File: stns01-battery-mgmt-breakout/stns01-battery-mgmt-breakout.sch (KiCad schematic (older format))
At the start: 0 parts

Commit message: Create schematic.
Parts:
- added B1: 3.7V, Wickerlib:UNDEFINED, symbol BATT-LIPO-3.7V-500MAH-JST-2PIN
- added C1, C3, C4: 2.2uF, Wickerlib:RLC-0603-SMD, symbol CAP-CER-2.2UF-10V-X7R-0603
- added C2: 4.7uF, Wickerlib:RLC-0603-SMD, symbol CAP-CER-4.7UF-6.3V-X7R-0603
- added J1: MICRO USB, Wickerlib:CONN-USB-MICRO-B-AMPHENOL-10118193-0001LF, symbol CONN-USB-MICRO-B-10118193
- added J2: PH, Wickerlib:CONN-JST-S2B-PH-SM4-TB, symbol HEADER-FEMALE-2POS-TH-1x02-JST-PH
- added J3: POWER PINS, Wickerlib:CONN-HEADER-STRAIGHT-P2.54MM-1x07, symbol HEADER-MALE-7POS-TH-1x07-P0.1IN
- added J4: CONTROL PINS, Wickerlib:CONN-HEADER-STRAIGHT-P2.54MM-1x07, symbol HEADER-MALE-7POS-TH-1x07-P0.1IN
- added LED1: RED, Wickerlib:LED-0603-SMD, symbol LED-RED-0603-SMT-HSMS-C191
- added R1: 0 ohm, Wickerlib:RLC-0603-SMD, symbol RES-0.0-JUMPER-1/8W-0603
- added R2, R5, R6: 10K, Wickerlib:RLC-0603-SMD, symbol RES-10K-1%-1/8W-0603
- added R3: NTC 10K, Wickerlib:RLC-0402-SMD, symbol THERM-NTC-10K-1%-0402
- added R4: 604, Wickerlib:RLC-0603-SMD, symbol RES-604-OHM-1%-1/10W-0603
- added S1: SHUNT, Wickerlib:CONN-HEADER-STRAIGHT-P2.54MM-1x03, symbol SWITCH_JUMPER_3PIN
- added S2: SLIDE, Wickerlib:SWITCH-ESWITCH-SLIDE-TH-EG1218, symbol SWITCH-SLIDE-SPDT-200MA-30V
- added U1: STNS01, Wickerlib:DFN-12-1EP-3x3MM-P0.45MM, symbol IC-LI-ION-BATT-CHARGER-LDO-STNS01-DFN12
- added U2: LDO REG 3.3V, Wickerlib:SOT-23-3, symbol IC-REG-LDO-3.3V-0.25A-MCP1703-SOT23A-3
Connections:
- net labels added: 3.1V, 3.3V, BAT_CEN, BAT_MS, BAT_NTC, BAT_SD, GND, LDO, SYS, TRANS, VBAT, VCC, VUSB, ~BAT_CHG
- wire segments 0 -> 57
- no-connect marks 0 -> 6
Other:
- note added: "100mA"
- note added: "250mA"
- note added: "BATTERY"
- note added: "BATTERY CONTROL"
- note added: "ON/OFF\nSWITCH"
- note added: "SYS is 5V with USB applied"
- note added: "TODO: 0603 NTC 10K"
- note added: "TODO: see if this is optional"
- note added: "USB"
- note added: "VOLTAGE \nREGULATOR"

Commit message: Generate BOM. Initial parts placement.
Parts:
- removed R3: NTC 10K, Wickerlib:RLC-0402-SMD, symbol THERM-NTC-10K-1%-0402
- added R3: NTC 10K, Wickerlib:RLC-0603-SMD, symbol THERM-NTC-10K-5%-0603
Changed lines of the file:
@@
 $EndComp
 $Comp
-L VUSB #PWR01
+L VUSB #PWR2
 U 1 1 58F8E338
 P 1700 1700
-F 0 "#PWR01" H 1700 1550 50  0001 C CNN
+F 0 "#PWR2" H 1700 1550 50  0001 C CNN
 F 1 "VUSB" H 1700 1840 50  0000 C CNN
 F 2 "" H 1700 1700 50  0000 C CNN
@@
 $EndComp
 $Comp
-L GND #PWR02
+L GND #PWR1
 U 1 1 58F8E351
 P 1625 2275
-F 0 "#PWR02" H 1625 2025 50  0001 C CNN
+F 0 "#PWR1" H 1625 2025 50  0001 C CNN
 F 1 "GND" H 1625 2125 50  0000 C CNN
 F 2 "" H 1625 2275 50  0000 C CNN
@@
 $EndComp
 $Comp
-L VBAT #PWR03
+L VBAT #PWR4
 U 1 1 58F8E938
 P 2700 2250
-F 0 "#PWR03" H 2700 2100 50  0001 C CNN
+F 0 "#PWR4" H 2700 2100 50  0001 C CNN
 F 1 "VBAT" H 2700 2390 50  0000 C CNN
 F 2 "" H 2700 2250 50  0000 C CNN
@@
 $EndComp
 $Comp
-L GND #PWR04
+L GND #PWR15
 U 1 1 58FA8587
 P 6725 2125
-F 0 "#PWR04" H 6725 1875 50  0001 C CNN
+F 0 "#PWR15" H 6725 1875 50  0001 C CNN
 F 1 "GND" H 6725 1975 50  0000 C CNN
 F 2 "" H 6725 2125 50  0000 C CNN
@@
 USB
 $Comp
-L GND #PWR05
+L GND #PWR5
 U 1 1 58FE6662
 P 2700 2700
-F 0 "#PWR05" H 2700 2450 50  0001 C CNN
+F 0 "#PWR5" H 2700 2450 50  0001 C CNN
 F 1 "GND" H 2700 2550 50  0000 C CNN
 F 2 "" H 2700 2700 50  0000 C CNN
@@
 $EndComp
 $Comp
-L GND #PWR06
+L GND #PWR3
 U 1 1 59019EDC
 P 2200 2150
-F 0 "#PWR06" H 2200 1900 50  0001 C CNN
+F 0 "#PWR3" H 2200 1900 50  0001 C CNN
 F 1 "GND" H 2200 2000 50  0000 C CNN
 F 2 "" H 2200 2150 50  0000 C CNN
@@
 $EndComp
 $Comp
-L GND #PWR07
+L GND #PWR8
 U 1 1 5901E800
 P 3750 2975
-F 0 "#PWR07" H 3750 2725 50  0001 C CNN
+F 0 "#PWR8" H 3750 2725 50  0001 C CNN
 F 1 "GND" H 3750 2825 50  0000 C CNN
 F 2 "" H 3750 2975 50  0000 C CNN
@@
 $EndComp
 $Comp
-L GND #PWR08
+L GND #PWR7
 U 1 1 59022473
 P 3500 2975
-F 0 "#PWR08" H 3500 2725 50  0001 C CNN
+F 0 "#PWR7" H 3500 2725 50  0001 C CNN
 F 1 "GND" H 3500 2825 50  0000 C CNN
 F 2 "" H 3500 2975 50  0000 C CNN
@@
 $EndComp
 $Comp
-L GND #PWR09
+L GND #PWR10
 U 1 1 59024679
 P 5650 2200
-F 0 "#PWR09" H 5650 1950 50  0001 C CNN
+F 0 "#PWR10" H 5650 1950 50  0001 C CNN
 F 1 "GND" H 5650 2050 50  0000 C CNN
 F 2 "" H 5650 2200 50  0000 C CNN
@@
 $EndComp
 $Comp
-L GND #PWR010
+L GND #PWR13
 U 1 1 59024867
 P 6050 2200
-F 0 "#PWR010" H 6050 1950 50  0001 C CNN
+F 0 "#PWR13" H 6050 1950 50  0001 C CNN
 F 1 "GND" H 6050 2050 50  0000 C CNN
 F 2 "" H 6050 2200 50  0000 C CNN
@@
 Text Label 4800 2825 0    50   ~ 0
 BAT_SD
-$Comp
-L THERM-NTC-10K-1%-0402 R3
-U 1 1 5902A870
-P 4825 3100
-F 0 "R3" H 4875 3150 50  0000 L CNN
-F 1 "NTC 10K" H 4875 3050 50  0000 L CNN
-F 2 "Wickerlib:RLC-0402-SMD" H 4825 2750 50  0001 C CIN
-F 3 "https://product.tdk.com/info/en/catalog/datasheets/tpd_ntc-thermistor_ntcg_en.pdf" H 4825 3100 5   0001 C CNN
-F 4 "NTC THERMISTOR 10K OHM 1% 0402" H 4825 2750 50  0001 C CIN "Description"
-F 5 "Samsung" H 4825 2750 50  0001 C CIN "MF_Name"
-F 6 "NTCG103JF103FT1" H 4825 2750 50  0001 C CIN "MF_PN"
-F 7 "Digikey" H 4825 2750 50  0001 C CIN "S1_Name"
-F 8 "445-2550-1-ND" H 4825 2750 50  0001 C CIN "S1_PN"
-	1    4825 3100
-	1    0    0    -1
-$EndComp
 $Comp
 L CAP-CER-4.7UF-6.3V-X7R-0603 C2
@@
 $EndComp
 $Comp
-L GND #PWR011
+L GND #PWR9
 U 1 1 5902C4A7
 P 4825 3200
-F 0 "#PWR011" H 4825 2950 50  0001 C CNN
+F 0 "#PWR9" H 4825 2950 50  0001 C CNN
 F 1 "GND" H 4825 3050 50  0000 C CNN
 F 2 "" H 4825 3200 50  0000 C CNN
@@
 $EndComp
 $Comp
-L GND #PWR012
+L GND #PWR6
 U 1 1 5903DF61
 P 3175 2600
-F 0 "#PWR012" H 3175 2350 50  0001 C CNN
+F 0 "#PWR6" H 3175 2350 50  0001 C CNN
 F 1 "GND" H 3175 2450 50  0000 C CNN
 F 2 "" H 3175 2600 50  0000 C CNN
@@
 $EndComp
 $Comp
-L VCC #PWR013
+L VCC #PWR16
 U 1 1 5906674F
 P 9100 1850
-F 0 "#PWR013" H 9100 1700 50  0001 C CNN
+F 0 "#PWR16" H 9100 1700 50  0001 C CNN
 F 1 "VCC" H 9100 1990 50  0000 C CNN
 F 2 "" H 9100 1850 50  0000 C CNN
@@
 	5775 5000 5775 5100
 $Comp
-L GND #PWR014
+L GND #PWR11
 U 1 1 5970EEFD
 P 5775 5100
-F 0 "#PWR014" H 5775 4850 50  0001 C CNN
+F 0 "#PWR11" H 5775 4850 50  0001 C CNN
 F 1 "GND" H 5775 4950 50  0000 C CNN
 F 2 "" H 5775 5100 50  0000 C CNN
@@
 	4750 5000 5100 5000
 $Comp
-L VCC #PWR015
+L VCC #PWR12
 U 1 1 59713110
 P 5800 4300
-F 0 "#PWR015" H 5800 4150 50  0001 C CNN
+F 0 "#PWR12" H 5800 4150 50  0001 C CNN
 F 1 "VCC" H 5800 4440 50  0000 C CNN
 F 2 "" H 5800 4300 50  0000 C CNN
@@
 $EndComp
 $Comp
-L GND #PWR016
+L GND #PWR14
 U 1 1 5971494F
 P 6125 3425
-F 0 "#PWR016" H 6125 3175 50  0001 C CNN
+F 0 "#PWR14" H 6125 3175 50  0001 C CNN
 F 1 "GND" H 6125 3275 50  0000 C CNN
 F 2 "" H 6125 3425 50  0000 C CNN
@@
 	1    0    0    -1
 $EndComp
+$Comp
+L THERM-NTC-10K-5%-0603 R3
+U 1 1 59715C0B
+P 4825 3100
+F 0 "R3" H 4875 3150 50  0000 L CNN
+F 1 "NTC 10K" H 4875 3050 50  0000 L CNN
+F 2 "Wickerlib:RLC-0603-SMD" H 4825 2750 50  0001 C CIN
+F 3 "https://product.tdk.com/info/en/catalog/datasheets/tpd_ntc-thermistor_ntcg_en.pdf" H 4825 3100 5   0001 C CNN
+F 4 "NTC THERMISTOR 10K OHM 5% 0603" H 4825 2750 50  0001 C CIN "Description"
+F 5 "TDK" H 4825 2750 50  0001 C CIN "MF_Name"
+F 6 "NTCG164BH103JT1" H 4825 2750 50  0001 C CIN "MF_PN"
+F 7 "Digikey" H 4825 2750 50  0001 C CIN "S1_Name"
+F 8 "445-174327-1-ND" H 4825 2750 50  0001 C CIN "S1_PN"
+	1    4825 3100
+	1    0    0    -1
+$EndComp

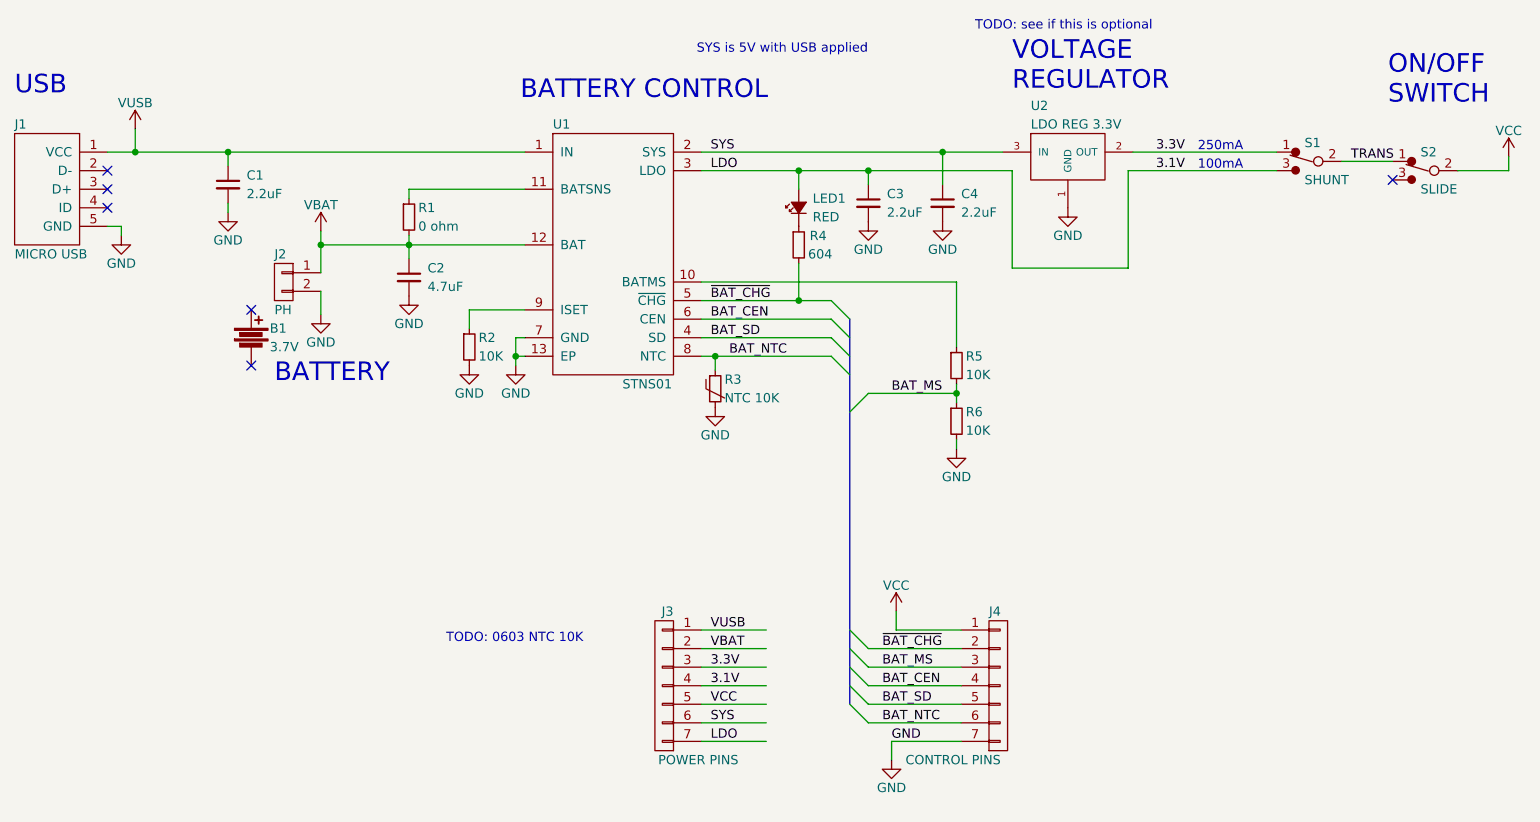
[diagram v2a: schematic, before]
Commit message: Release v1.0 STNS01 battery breakout, needs tested.
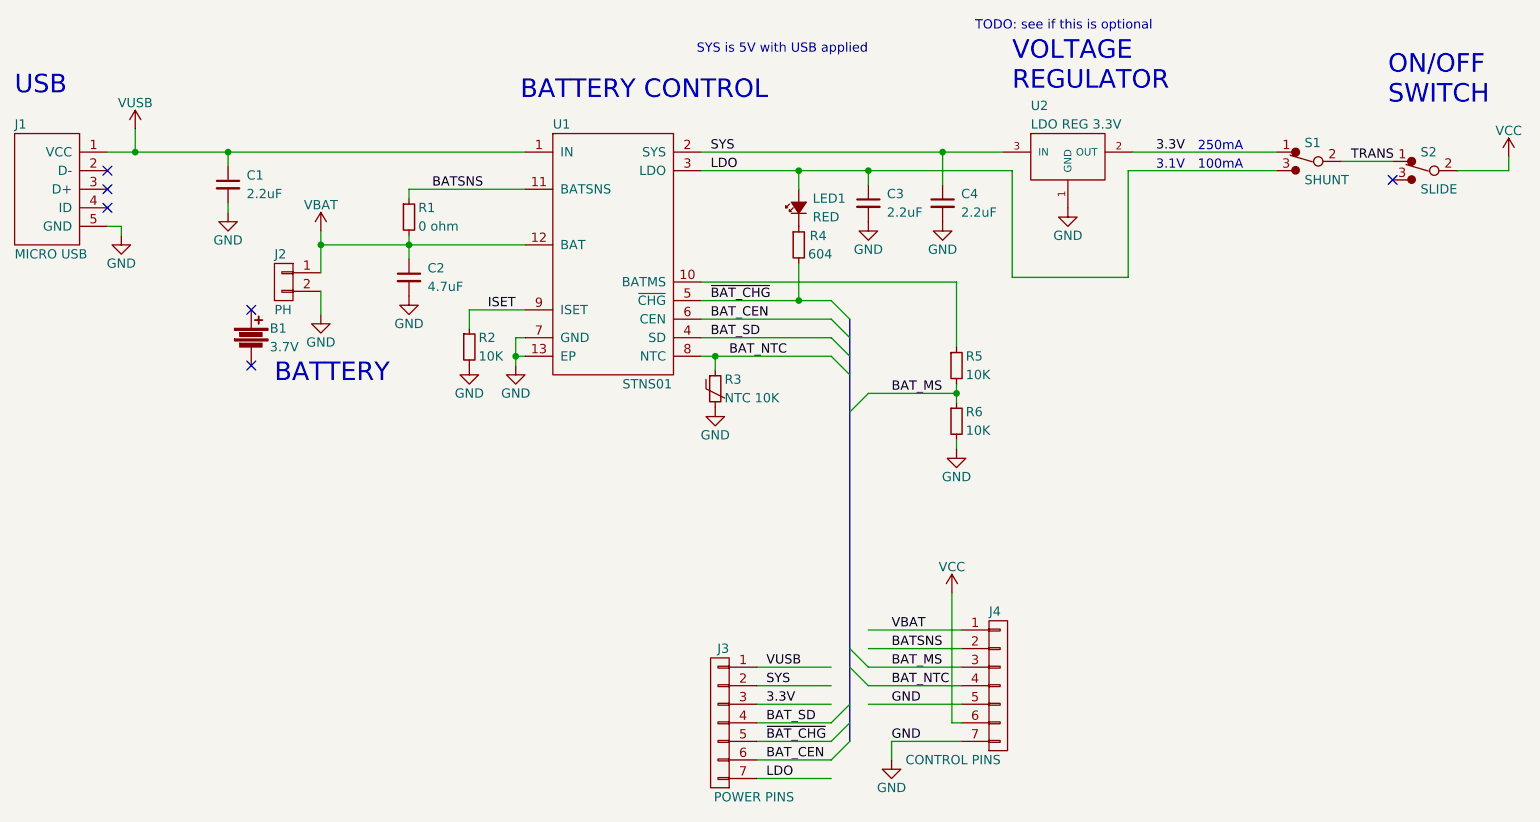
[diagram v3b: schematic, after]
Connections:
- net labels added: BATSNS, ISET
- net labels removed: 3.1V
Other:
- note added: "3.1V"
- note removed: "TODO: 0603 NTC 10K"
- moved on the sheet: J3
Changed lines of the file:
@@
 EESchema Schematic File Version 2
 LIBS:wickerlib
+LIBS:stns01-battery-mgmt-breakout-cache
 EELAYER 25 0
 EELAYER END
@@
 $EndComp
 $Comp
-L VUSB #PWR2
+L VUSB #PWR01
 U 1 1 58F8E338
 P 1700 1700
-F 0 "#PWR2" H 1700 1550 50  0001 C CNN
+F 0 "#PWR01" H 1700 1550 50  0001 C CNN
 F 1 "VUSB" H 1700 1840 50  0000 C CNN
 F 2 "" H 1700 1700 50  0000 C CNN
@@
 $EndComp
 $Comp
-L GND #PWR1
+L GND #PWR02
 U 1 1 58F8E351
 P 1625 2275
-F 0 "#PWR1" H 1625 2025 50  0001 C CNN
+F 0 "#PWR02" H 1625 2025 50  0001 C CNN
 F 1 "GND" H 1625 2125 50  0000 C CNN
 F 2 "" H 1625 2275 50  0000 C CNN
@@
 $EndComp
 $Comp
-L VBAT #PWR4
+L VBAT #PWR03
 U 1 1 58F8E938
 P 2700 2250
-F 0 "#PWR4" H 2700 2100 50  0001 C CNN
+F 0 "#PWR03" H 2700 2100 50  0001 C CNN
 F 1 "VBAT" H 2700 2390 50  0000 C CNN
 F 2 "" H 2700 2250 50  0000 C CNN
@@
 $EndComp
 $Comp
-L GND #PWR15
+L GND #PWR04
 U 1 1 58FA8587
 P 6725 2125
-F 0 "#PWR15" H 6725 1875 50  0001 C CNN
+F 0 "#PWR04" H 6725 1875 50  0001 C CNN
 F 1 "GND" H 6725 1975 50  0000 C CNN
 F 2 "" H 6725 2125 50  0000 C CNN
@@
 USB
 $Comp
-L GND #PWR5
+L GND #PWR05
 U 1 1 58FE6662
 P 2700 2700
-F 0 "#PWR5" H 2700 2450 50  0001 C CNN
+F 0 "#PWR05" H 2700 2450 50  0001 C CNN
 F 1 "GND" H 2700 2550 50  0000 C CNN
 F 2 "" H 2700 2700 50  0000 C CNN
@@
 $EndComp
 $Comp
-L GND #PWR3
+L GND #PWR06
 U 1 1 59019EDC
 P 2200 2150
-F 0 "#PWR3" H 2200 1900 50  0001 C CNN
+F 0 "#PWR06" H 2200 1900 50  0001 C CNN
 F 1 "GND" H 2200 2000 50  0000 C CNN
 F 2 "" H 2200 2150 50  0000 C CNN
@@
 $EndComp
 $Comp
-L GND #PWR8
+L GND #PWR07
 U 1 1 5901E800
 P 3750 2975
-F 0 "#PWR8" H 3750 2725 50  0001 C CNN
+F 0 "#PWR07" H 3750 2725 50  0001 C CNN
 F 1 "GND" H 3750 2825 50  0000 C CNN
 F 2 "" H 3750 2975 50  0000 C CNN
@@
 $EndComp
 $Comp
-L GND #PWR7
+L GND #PWR08
 U 1 1 59022473
 P 3500 2975
-F 0 "#PWR7" H 3500 2725 50  0001 C CNN
+F 0 "#PWR08" H 3500 2725 50  0001 C CNN
 F 1 "GND" H 3500 2825 50  0000 C CNN
 F 2 "" H 3500 2975 50  0000 C CNN
@@
 $EndComp
 $Comp
-L GND #PWR10
+L GND #PWR09
 U 1 1 59024679
 P 5650 2200
-F 0 "#PWR10" H 5650 1950 50  0001 C CNN
+F 0 "#PWR09" H 5650 1950 50  0001 C CNN
 F 1 "GND" H 5650 2050 50  0000 C CNN
 F 2 "" H 5650 2200 50  0000 C CNN
@@
 $EndComp
 $Comp
-L GND #PWR13
+L GND #PWR010
 U 1 1 59024867
 P 6050 2200
-F 0 "#PWR13" H 6050 1950 50  0001 C CNN
+F 0 "#PWR010" H 6050 1950 50  0001 C CNN
 F 1 "GND" H 6050 2050 50  0000 C CNN
 F 2 "" H 6050 2200 50  0000 C CNN
@@
 $EndComp
 $Comp
-L GND #PWR9
+L GND #PWR011
 U 1 1 5902C4A7
 P 4825 3200
-F 0 "#PWR9" H 4825 2950 50  0001 C CNN
+F 0 "#PWR011" H 4825 2950 50  0001 C CNN
 F 1 "GND" H 4825 3050 50  0000 C CNN
 F 2 "" H 4825 3200 50  0000 C CNN
@@
 $EndComp
 $Comp
-L GND #PWR6
+L GND #PWR012
 U 1 1 5903DF61
 P 3175 2600
-F 0 "#PWR6" H 3175 2350 50  0001 C CNN
+F 0 "#PWR012" H 3175 2350 50  0001 C CNN
 F 1 "GND" H 3175 2450 50  0000 C CNN
 F 2 "" H 3175 2600 50  0000 C CNN
@@
 Text Label 4800 1825 0    50   ~ 0
 SYS
-Text Notes 6225 1175 0    50   ~ 0
-TODO: see if this is optional
 Text Label 7200 1825 0    50   ~ 0
 3.3V
-Text Label 7200 1925 0    50   ~ 0
-3.1V
 Text Notes 7425 1825 0    50   ~ 0
 250mA
@@
 	7050 1925 7850 1925
 Wire Wire Line
-	7050 2450 7050 1925
-Wire Wire Line
-	6425 2450 7050 2450
-Wire Wire Line
 	7075 1825 7850 1825
-Wire Wire Line
-	6425 1925 6425 2450
 Connection ~ 6050 1825
 Wire Wire Line
@@
 $EndComp
 $Comp
-L VCC #PWR16
+L VCC #PWR013
 U 1 1 5906674F
 P 9100 1850
-F 0 "#PWR16" H 9100 1700 50  0001 C CNN
+F 0 "#PWR013" H 9100 1700 50  0001 C CNN
 F 1 "VCC" H 9100 1990 50  0000 C CNN
 F 2 "" H 9100 1850 50  0000 C CNN
@@
 Text Notes 8450 1575 0    100  ~ 0
 ON/OFF\nSWITCH
-Text Label 4800 4400 0    50   ~ 0
+Text Label 5100 4600 0    50   ~ 0
 VUSB
-Text Label 4800 4600 0    50   ~ 0
+Text Label 5100 4800 0    50   ~ 0
 3.3V
-Text Label 4800 4700 0    50   ~ 0
-3.1V
-Text Label 4800 4800 0    50   ~ 0
-VCC
-Text Label 4800 4500 0    50   ~ 0
+Text Label 5775 4400 0    50   ~ 0
 VBAT
-Text Label 4800 4900 0    50   ~ 0
+Text Label 5100 4700 0    50   ~ 0
 SYS
-Text Label 4800 5000 0    50   ~ 0
+Text Label 5100 5200 0    50   ~ 0
 LDO
-Text Label 5725 4500 0    50   ~ 0
+Text Label 5100 5000 0    50   ~ 0
 ~BAT_CHG
-Text Label 5725 4600 0    50   ~ 0
+Text Label 5775 4600 0    50   ~ 0
 BAT_MS
-Text Label 5725 4700 0    50   ~ 0
+Text Label 5100 5100 0    50   ~ 0
 BAT_CEN
-Text Label 5725 4800 0    50   ~ 0
+Text Label 5100 4900 0    50   ~ 0
 BAT_SD
-Text Label 5725 4900 0    50   ~ 0
+Text Label 5775 4700 0    50   ~ 0
 BAT_NTC
-Text Notes 3375 4475 0    50   ~ 0
-TODO: 0603 NTC 10K
 Connection ~ 6125 3125
 Wire Bus Line
-	5550 2725 5550 4800
-Entry Wire Line
-	5550 4800 5650 4900
-Wire Wire Line
-	5650 4900 6150 4900
-Entry Wire Line
-	5550 4700 5650 4800
+	5550 2725 5550 5000
+Entry Wire Line
+	5450 4900 5550 4800
+Wire Wire Line
+	5650 4400 6150 4400
+Entry Wire Line
+	5550 4500 5650 4600
 Entry Wire Line
 	5550 4600 5650 4700
-Entry Wire Line
-	5550 4500 5650 4600
-Entry Wire Line
-	5550 4400 5650 4500
 Text Label 5775 5000 0    50   ~ 0
 GND
@@
 	5775 5000 5775 5100
 $Comp
-L GND #PWR11
+L GND #PWR014
 U 1 1 5970EEFD
 P 5775 5100
-F 0 "#PWR11" H 5775 4850 50  0001 C CNN
+F 0 "#PWR014" H 5775 4850 50  0001 C CNN
 F 1 "GND" H 5775 4950 50  0000 C CNN
 F 2 "" H 5775 5100 50  0000 C CNN
@@
 $EndComp
 Wire Wire Line
-	6150 4400 5800 4400
-Wire Wire Line
-	5800 4400 5800 4300
+	6100 4200 6100 4900
 $Comp
 L HEADER-MALE-7POS-TH-1x07-P0.1IN J3
 U 1 1 59711491
-P 4550 4700
-F 0 "J3" H 4500 5100 50  0000 L CNN
-F 1 "POWER PINS" H 4150 4300 50  0000 L CNN
-F 2 "Wickerlib:CONN-HEADER-STRAIGHT-P2.54MM-1x07" H 4550 4350 50  0001 C CIN
-F 3 "https://cdn.harwin.com/pdfs/60page140.pdf" H 4550 4700 5   0001 C CNN
-F 4 "HEADER MALE 7POS TH 1x07 0.1IN" H 4550 4350 50  0001 C CIN "Description"
-F 5 "Harwin" H 4550 4350 50  0001 C CIN "MF_Name"
-F 6 "M20-9992046" H 4550 4350 50  0001 C CIN "MF_PN"
-F 7 "Digikey" H 4550 4350 50  0001 C CIN "S1_Name"
-F 8 "952-1902-ND" H 4550 4350 50  0001 C CIN "S1_PN"
-	1    4550 4700
+P 4850 4900
+F 0 "J3" H 4800 5300 50  0000 L CNN
+F 1 "POWER PINS" H 4450 4500 50  0000 L CNN
+F 2 "Wickerlib:CONN-HEADER-STRAIGHT-P2.54MM-1x07" H 4850 4550 50  0001 C CIN
+F 3 "https://cdn.harwin.com/pdfs/60page140.pdf" H 4850 4900 5   0001 C CNN
+F 4 "HEADER MALE 7POS TH 1x07 0.1IN" H 4850 4550 50  0001 C CIN "Description"
+F 5 "Harwin" H 4850 4550 50  0001 C CIN "MF_Name"
+F 6 "M20-9992046" H 4850 4550 50  0001 C CIN "MF_PN"
+F 7 "Digikey" H 4850 4550 50  0001 C CIN "S1_Name"
+F 8 "952-1902-ND" H 4850 4550 50  0001 C CIN "S1_PN"
+	1    4850 4900
 	-1   0    0    -1
 $EndComp
 Wire Wire Line
-	4750 4400 5100 4400
-Wire Wire Line
-	4750 4500 5100 4500
-Wire Wire Line
-	4750 4600 5100 4600
-Wire Wire Line
-	4750 4700 5100 4700
-Wire Wire Line
-	4750 4800 5100 4800
-Wire Wire Line
-	4750 4900 5100 4900
-Wire Wire Line
-	4750 5000 5100 5000
-$Comp
-L VCC #PWR12
+	5050 4600 5450 4600
+Wire Wire Line
+	5050 4700 5450 4700
+Wire Wire Line
+	5050 4800 5450 4800
+Wire Wire Line
+	5050 4900 5450 4900
+Wire Wire Line
+	5050 5000 5450 5000
+Wire Wire Line
+	5050 5100 5450 5100
+Wire Wire Line
+	5050 5200 5450 5200
+$Comp
+L VCC #PWR015
 U 1 1 59713110
-P 5800 4300
-F 0 "#PWR12" H 5800 4150 50  0001 C CNN
-F 1 "VCC" H 5800 4440 50  0000 C CNN
-F 2 "" H 5800 4300 50  0000 C CNN
-F 3 "" H 5800 4300 50  0000 C CNN
-	1    5800 4300
-	1    0    0    -1
-$EndComp
-$Comp
-L GND #PWR14
+P 6100 4200
+F 0 "#PWR015" H 6100 4050 50  0001 C CNN
+F 1 "VCC" H 6100 4340 50  0000 C CNN
+F 2 "" H 6100 4200 50  0000 C CNN
+F 3 "" H 6100 4200 50  0000 C CNN
+	1    6100 4200
+	1    0    0    -1
+$EndComp
+$Comp
+L GND #PWR016
 U 1 1 5971494F
 P 6125 3425
-F 0 "#PWR14" H 6125 3175 50  0001 C CNN
+F 0 "#PWR016" H 6125 3175 50  0001 C CNN
 F 1 "GND" H 6125 3275 50  0000 C CNN
 F 2 "" H 6125 3425 50  0000 C CNN
@@
 	1    0    0    -1
 $EndComp
+Text Notes 7200 1925 0    50   ~ 0
+3.1V
+Text Label 3300 2025 0    50   ~ 0
+BATSNS
+Text Label 3600 2675 0    50   ~ 0
+ISET
+Wire Wire Line
+	7050 1925 7050 2500
+Wire Wire Line
+	7050 2500 6425 2500
+Wire Wire Line
+	6425 2500 6425 1925
+Wire Wire Line
+	6100 4900 6150 4900
+Entry Wire Line
+	5450 5000 5550 4900
+Entry Wire Line
+	5450 5100 5550 5000
+Text Label 5775 4800 0    50   ~ 0
+GND
+Text Label 5775 4500 0    50   ~ 0
+BATSNS
+Text Notes 6225 1175 0    50   ~ 0
+TODO: see if this is optional
 $EndSCHEMATC
